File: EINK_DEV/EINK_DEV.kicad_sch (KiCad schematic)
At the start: 33 parts, among them J1 FPC, J2 USB_B_Micro, Q1 NMOS, U1 STM32WB55CEUx, U2 TP4056-42-ESOP8

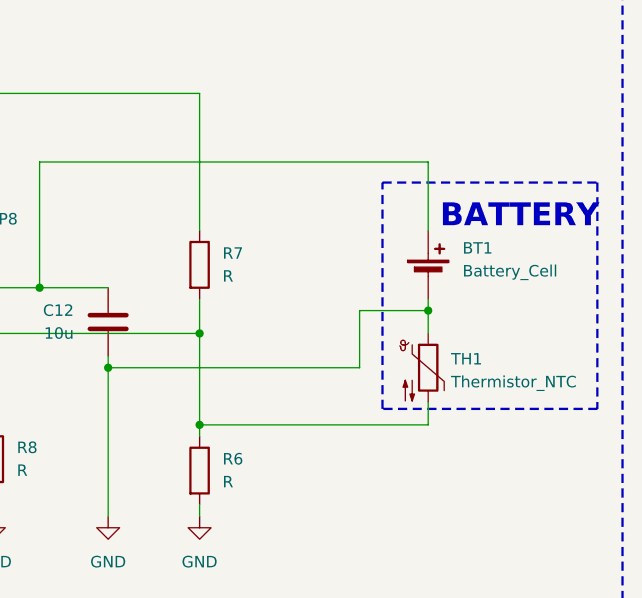
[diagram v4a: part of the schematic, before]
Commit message: Add connector instead of battery
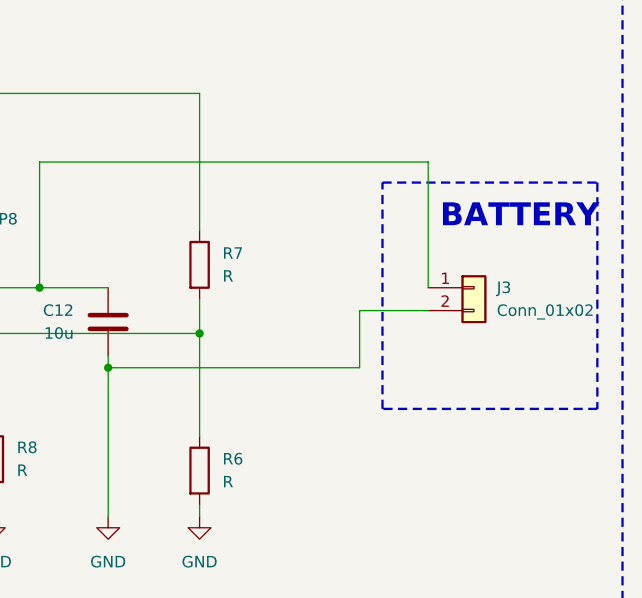
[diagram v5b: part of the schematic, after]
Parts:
- removed BT1: Battery_Cell, symbol Device:Battery_Cell
- removed TH1: Thermistor_NTC, symbol Device:Thermistor_NTC
- added J3: Conn_01x02, symbol Connector_Generic:Conn_01x02
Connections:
- net GND: now also J3.2 (Pin_2)
- net at C12.2, U2.5 (BAT): now also J3.1 (Pin_1)
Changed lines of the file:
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@@
 	)
 	(junction
-		(at 237.49 100.33)
-		(diameter 0)
-		(color 0 0 0 0)
-	)
-	(junction
 		(at 237.49 90.17)
 		(diameter 0)
@@
 	)
 	(junction
-		(at 262.89 87.63)
-		(diameter 0)
-		(color 0 0 0 0)
-	)
-	(junction
 		(at 219.71 85.09)
 		(diameter 0)
@@
 	(wire
 		(pts
-			(xy 237.49 100.33) (xy 237.49 101.6)
+			(xy 237.49 90.17) (xy 237.49 101.6)
 		)
 		(stroke
@@
 	(wire
 		(pts
-			(xy 262.89 86.36) (xy 262.89 87.63)
-		)
-		(stroke
-			(width 0)
-			(type default)
-		)
-	)
-	(wire
-		(pts
 			(xy 189.23 92.71) (xy 160.02 92.71)
 		)
@@
 	(wire
 		(pts
-			(xy 262.89 87.63) (xy 262.89 90.17)
-		)
-		(stroke
-			(width 0)
-			(type default)
-		)
-	)
-	(wire
-		(pts
 			(xy 99.06 149.86) (xy 99.06 152.4)
 		)
@@
 	(wire
 		(pts
-			(xy 237.49 90.17) (xy 237.49 100.33)
-		)
-		(stroke
-			(width 0)
-			(type default)
-		)
-	)
-	(wire
-		(pts
 			(xy 160.02 63.5) (xy 160.02 69.85)
 		)
@@
 	(wire
 		(pts
-			(xy 237.49 100.33) (xy 262.89 100.33)
-		)
-		(stroke
-			(width 0)
-			(type default)
-		)
-	)
-	(wire
-		(pts
-			(xy 262.89 100.33) (xy 262.89 97.79)
-		)
-		(stroke
-			(width 0)
-			(type default)
-		)
-	)
-	(wire
-		(pts
 			(xy 154.94 186.69) (xy 158.75 186.69)
 		)
@@
 	(wire
 		(pts
-			(xy 262.89 71.12) (xy 262.89 78.74)
+			(xy 262.89 71.12) (xy 262.89 85.09)
 		)
 		(stroke
@@
 	)
 	(symbol
-		(lib_id "Device:Thermistor_NTC")
-		(at 262.89 93.98 0)
-		(unit 1)
-		(exclude_from_sim no)
-		(in_bom yes)
-		(on_board yes)
-		(dnp no)
-		(fields_autoplaced yes)
-		(property "Reference" "TH1"
-			(at 265.43 93.0274 0)
-			(effects
-				(font
-					(size 1.27 1.27)
-				)
-				(justify left)
-			)
-		)
-		(property "Value" "Thermistor_NTC"
-			(at 265.43 95.5674 0)
-			(effects
-				(font
-					(size 1.27 1.27)
-				)
-				(justify left)
-			)
-		)
-		(property "Footprint" ""
-			(at 262.89 92.71 0)
-			(effects
-				(font
-					(size 1.27 1.27)
-				)
-				(hide yes)
-			)
-		)
-		(property "Datasheet" "~"
-			(at 262.89 92.71 0)
-			(effects
-				(font
-					(size 1.27 1.27)
-				)
-				(hide yes)
-			)
-		)
-		(property "Description" "Temperature dependent resistor, negative temperature coefficient"
-			(at 262.89 93.98 0)
-			(effects
-				(font
-					(size 1.27 1.27)
-				)
-				(hide yes)
-			)
-		)
-		(pin "1"
-		)
-		(pin "2"
-		)
-		(instances
-			(project ""
-				(path "/21ffd272-94a2-4b6a-9954-5d1217824b1f"
-					(reference "TH1")
-					(unit 1)
-				)
-			)
-		)
-	)
-	(symbol
 		(lib_id "Device:D")
 		(at 90.17 152.4 0)
@@
 	)
 	(symbol
-		(lib_id "Device:Battery_Cell")
-		(at 262.89 83.82 0)
-		(unit 1)
-		(exclude_from_sim no)
-		(in_bom yes)
-		(on_board yes)
-		(dnp no)
-		(fields_autoplaced yes)
-		(property "Reference" "BT1"
-			(at 266.7 80.7084 0)
-			(effects
-				(font
-					(size 1.27 1.27)
-				)
-				(justify left)
-			)
-		)
-		(property "Value" "Battery_Cell"
-			(at 266.7 83.2484 0)
-			(effects
-				(font
-					(size 1.27 1.27)
-				)
-				(justify left)
-			)
-		)
-		(property "Footprint" ""
-			(at 262.89 82.296 90)
-			(effects
-				(font
-					(size 1.27 1.27)
-				)
-				(hide yes)
-			)
-		)
-		(property "Datasheet" "~"
-			(at 262.89 82.296 90)
-			(effects
-				(font
-					(size 1.27 1.27)
-				)
-				(hide yes)
-			)
-		)
-		(property "Description" "Single-cell battery"
-			(at 262.89 83.82 0)
-			(effects
-				(font
-					(size 1.27 1.27)
-				)
-				(hide yes)
-			)
-		)
-		(pin "1"
-		)
-		(pin "2"
-		)
-		(instances
-			(project ""
-				(path "/21ffd272-94a2-4b6a-9954-5d1217824b1f"
-					(reference "BT1")
-					(unit 1)
-				)
-			)
-		)
-	)
-	(symbol
 		(lib_id "Device:C")
 		(at 227.33 88.9 0)
@@
 					(unit 1)
 				)
+			)
+		)
+	)
+	(symbol
+		(lib_id "Connector_Generic:Conn_01x02")
+		(at 267.97 85.09 0)
+		(unit 1)
+		(exclude_from_sim no)
+		(in_bom yes)
+		(on_board yes)
+		(dnp no)
+		(fields_autoplaced yes)
+		(property "Reference" "J3"
+			(at 270.51 85.0899 0)
+			(effects
+				(font
+					(size 1.27 1.27)
+				)
+				(justify left)
+			)
+		)
+		(property "Value" "Conn_01x02"
+			(at 270.51 87.6299 0)
+			(effects
+				(font
+					(size 1.27 1.27)
+				)
+				(justify left)
+			)
+		)
+		(property "Footprint" ""
+			(at 267.97 85.09 0)
+			(effects
+				(font
+					(size 1.27 1.27)
+				)
+				(hide yes)
+			)
+		)
+		(property "Datasheet" "~"
+			(at 267.97 85.09 0)
+			(effects
+				(font
+					(size 1.27 1.27)
+				)
+				(hide yes)
+			)
+		)
+		(property "Description" "Generic connector, single row, 01x02, script generated (kicad-library-utils/schlib/autogen/connector/)"
+			(at 267.97 85.09 0)
+			(effects
+				(font
+					(size 1.27 1.27)
+				)
+				(hide yes)
+			)
+		)
+		(pin "1"
+		)
+		(pin "2"
+		)
+		(instances
+			(project ""
+				(path "/21ffd272-94a2-4b6a-9954-5d1217824b1f"
+					(reference "J3")
+					(unit 1)
+				)

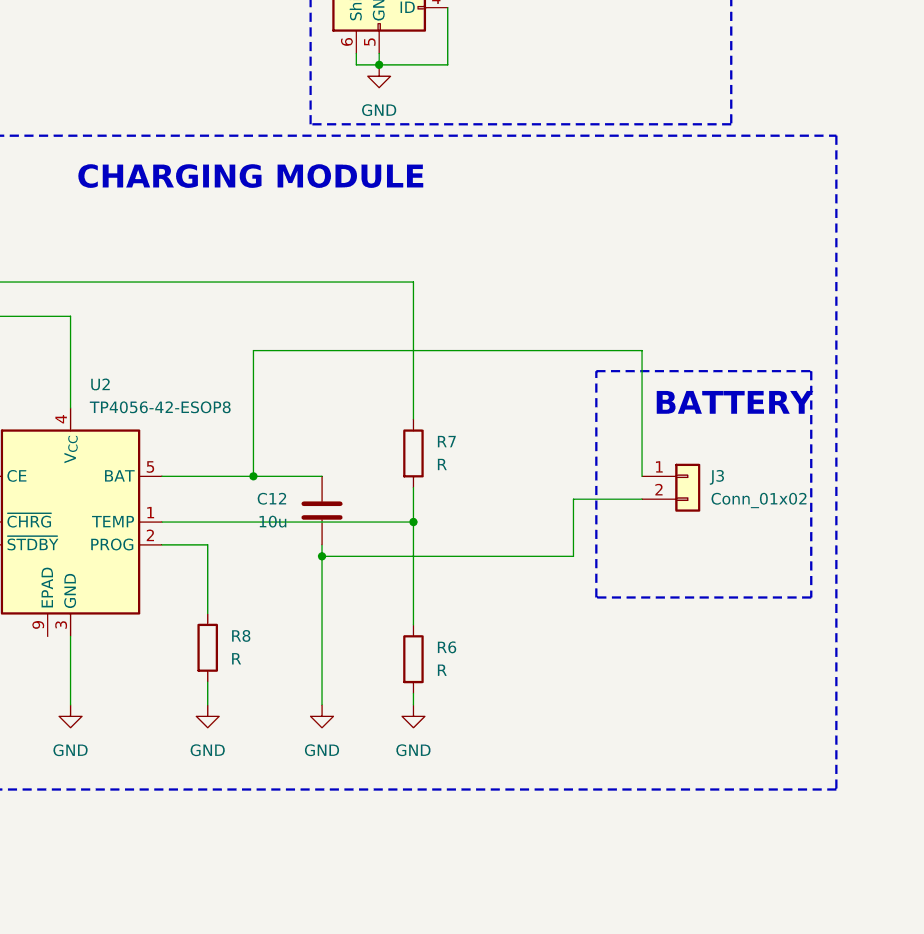
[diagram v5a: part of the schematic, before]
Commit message: Add options for baterry connector
2Pin and 3Pin Connector are available. Depends on a jumper placing.
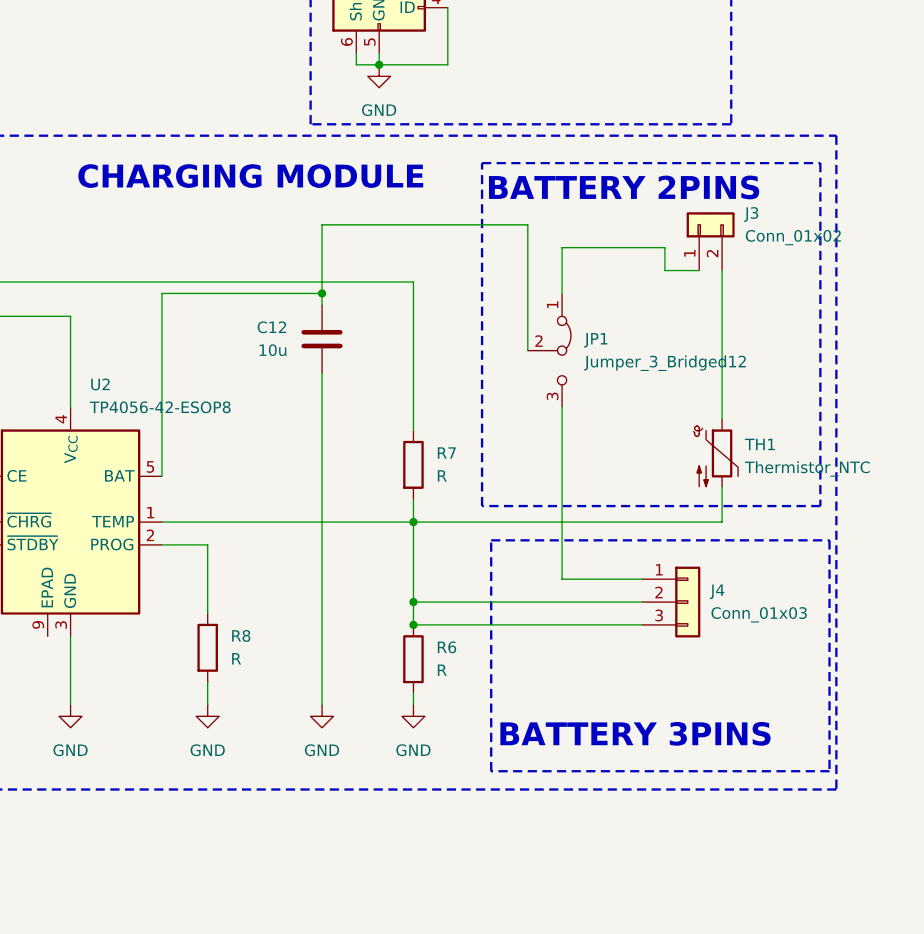
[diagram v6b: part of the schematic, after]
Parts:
- added J4: Conn_01x03, symbol Connector_Generic:Conn_01x03
- added JP1: Jumper_3_Bridged12, symbol Jumper:Jumper_3_Bridged12
- added TH1: Thermistor_NTC, symbol Device:Thermistor_NTC
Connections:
- net GND: no longer J3.2 (Pin_2)
- net at R6.1, R7.2, U2.1 (TEMP): now also J4.2 (Pin_2), J4.3 (Pin_3), TH1.2
- net at C12.2, U2.5 (BAT): now also JP1.2 (C); no longer J3.1 (Pin_1)
- new net: J3.1 (Pin_1), JP1.1 (A)
- new net: J3.2 (Pin_2), TH1.1
- new net: J4.1 (Pin_1), JP1.3 (B)
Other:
- note added: "BATTERY 2PINS"
- note added: "BATTERY 3PINS"
- note removed: "BATTERY"
- moved on the sheet: C12, R7

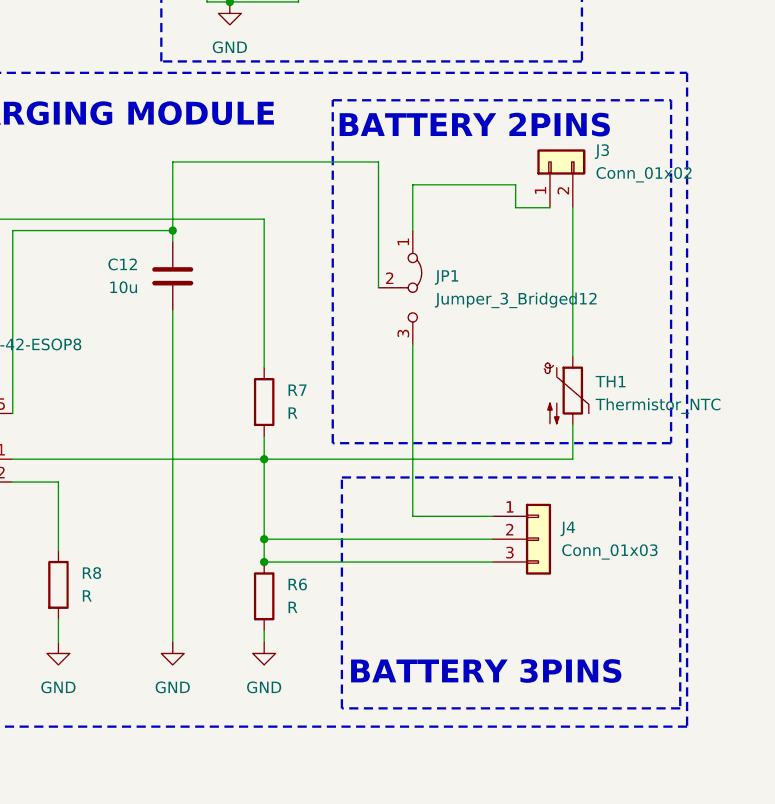
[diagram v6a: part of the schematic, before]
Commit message: Add onnections from battery to BAT pin
Add connections from 2 and 3Pin connectors to BAT pin.
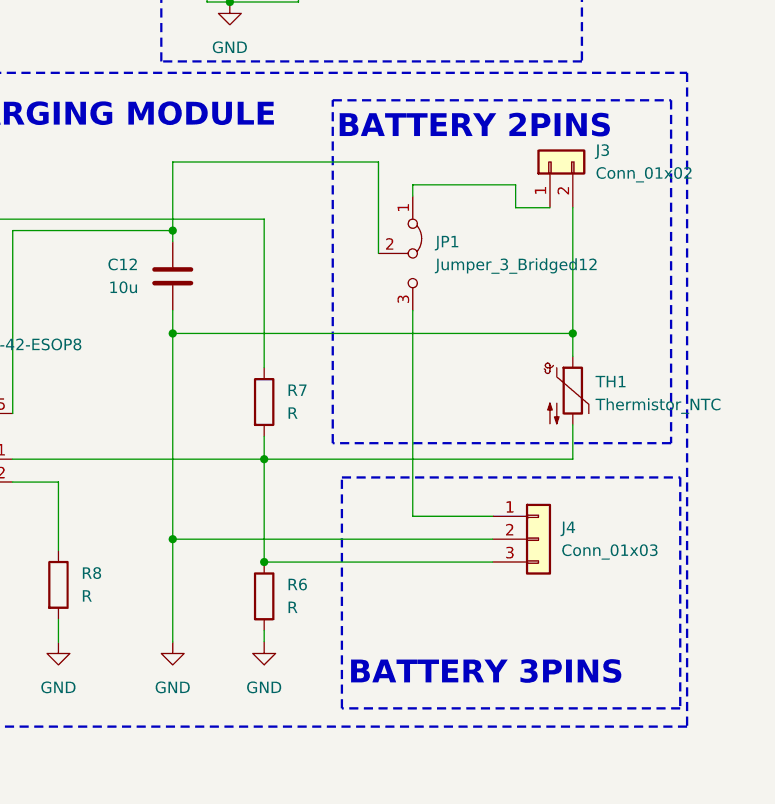
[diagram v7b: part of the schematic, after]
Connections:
- net GND: now also J3.2 (Pin_2), J4.2 (Pin_2), TH1.1
- net at J4.3 (Pin_3), R6.1, R7.2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: no longer J4.2 (Pin_2)
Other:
- moved on the sheet: JP1
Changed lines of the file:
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@@
 	)
 	(junction
+		(at 227.33 99.06)
+		(diameter 0)
+		(color 0 0 0 0)
+	)
+	(junction
 		(at 69.85 179.07)
 		(diameter 0)
@@
 	)
 	(junction
-		(at 237.49 99.06)
+		(at 271.78 76.2)
+		(diameter 0)
+		(color 0 0 0 0)
+	)
+	(junction
+		(at 227.33 76.2)
 		(diameter 0)
 		(color 0 0 0 0)
@@
 	(wire
 		(pts
-			(xy 250.19 57.15) (xy 250.19 71.12)
+			(xy 250.19 57.15) (xy 250.19 67.31)
 		)
 		(stroke
@@
 	(wire
 		(pts
+			(xy 227.33 99.06) (xy 227.33 110.49)
+		)
+		(stroke
+			(width 0)
+			(type default)
+		)
+	)
+	(wire
+		(pts
 			(xy 154.94 179.07) (xy 158.75 179.07)
 		)
@@
 	(wire
 		(pts
-			(xy 237.49 99.06) (xy 262.89 99.06)
+			(xy 254 59.69) (xy 254 60.96)
 		)
 		(stroke
@@
 	(wire
 		(pts
-			(xy 254 59.69) (xy 254 64.77)
+			(xy 154.94 130.81) (xy 158.75 130.81)
 		)
 		(stroke
@@
 	(wire
 		(pts
-			(xy 154.94 130.81) (xy 158.75 130.81)
+			(xy 99.06 144.78) (xy 99.06 142.24)
 		)
 		(stroke
@@
 	(wire
 		(pts
-			(xy 99.06 144.78) (xy 99.06 142.24)
+			(xy 160.02 87.63) (xy 160.02 92.71)
 		)
 		(stroke
@@
 	(wire
 		(pts
-			(xy 160.02 87.63) (xy 160.02 92.71)
+			(xy 124.46 166.37) (xy 133.35 166.37)
 		)
 		(stroke
@@
 	(wire
 		(pts
-			(xy 124.46 166.37) (xy 133.35 166.37)
+			(xy 254 59.69) (xy 265.43 59.69)
 		)
 		(stroke
@@
 	(wire
 		(pts
-			(xy 254 59.69) (xy 265.43 59.69)
+			(xy 173.99 78.74) (xy 173.99 80.01)
 		)
 		(stroke
@@
 	(wire
 		(pts
-			(xy 173.99 78.74) (xy 173.99 80.01)
+			(xy 227.33 76.2) (xy 271.78 76.2)
 		)
 		(stroke
@@
 	(wire
 		(pts
-			(xy 254 77.47) (xy 254 96.52)
+			(xy 254 73.66) (xy 254 96.52)
 		)
 		(stroke
@@
 	(wire
 		(pts
-			(xy 237.49 90.17) (xy 237.49 99.06)
+			(xy 237.49 90.17) (xy 237.49 101.6)
 		)
 		(stroke
@@
 	(wire
 		(pts
+			(xy 227.33 99.06) (xy 262.89 99.06)
+		)
+		(stroke
+			(width 0)
+			(type default)
+		)
+	)
+	(wire
+		(pts
 			(xy 138.43 179.07) (xy 144.78 179.07)
 		)
@@
 	(wire
 		(pts
-			(xy 227.33 73.66) (xy 227.33 110.49)
+			(xy 227.33 73.66) (xy 227.33 76.2)
 		)
 		(stroke
@@
 	(wire
 		(pts
-			(xy 271.78 62.23) (xy 271.78 78.74)
+			(xy 271.78 62.23) (xy 271.78 76.2)
 		)
 		(stroke
@@
 	(wire
 		(pts
-			(xy 237.49 99.06) (xy 237.49 101.6)
+			(xy 154.94 161.29) (xy 158.75 161.29)
 		)
 		(stroke
@@
 	(wire
 		(pts
-			(xy 154.94 161.29) (xy 158.75 161.29)
+			(xy 124.46 173.99) (xy 128.27 173.99)
 		)
 		(stroke
@@
 	(wire
 		(pts
-			(xy 124.46 173.99) (xy 128.27 173.99)
+			(xy 227.33 76.2) (xy 227.33 99.06)
 		)
 		(stroke
@@
 		)
 	)
+	(wire
+		(pts
+			(xy 271.78 76.2) (xy 271.78 78.74)
+		)
+		(stroke
+			(width 0)
+			(type default)
+		)
+	)
 	(global_label "VGH"
 		(shape bidirectional)
@@
 	(symbol
 		(lib_id "Jumper:Jumper_3_Bridged12")
-		(at 254 71.12 270)
+		(at 254 67.31 270)
 		(unit 1)
 		(exclude_from_sim no)
@@
 		(on_board yes)
 		(dnp no)
-		(fields_autoplaced yes)
 		(property "Reference" "JP1"
-			(at 256.54 69.8499 90)
+			(at 256.54 66.0399 90)
 			(effects
 				(font
@@
 		)
 		(property "Value" "Jumper_3_Bridged12"
-			(at 256.54 72.3899 90)
+			(at 256.54 68.5799 90)
 			(effects
 				(font
@@
 		)
 		(property "Footprint" ""
-			(at 254 71.12 0)
+			(at 254 67.31 0)
 			(effects
 				(font
@@
 		)
 		(property "Datasheet" "~"
-			(at 254 71.12 0)
+			(at 254 67.31 0)
 			(effects
 				(font
@@
 		)
 		(property "Description" "Jumper, 3-pole, pins 1+2 closed/bridged"
-			(at 254 71.12 0)
+			(at 254 67.31 0)
 			(effects
 				(font

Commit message: Added BATT protection
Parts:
- added C13: ~, symbol Device:C
- added R10: ~, symbol Device:R
- added R9: R, symbol Device:R
- added U3: DW01A, Package_TO_SOT_SMD:SOT-23-6, symbol Battery_Management:DW01A
- added U4: ~, symbol Battery_Management:FS8205A
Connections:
- net GND: now also C13.2, U3.6 (GND), U4.1 (S1)
- net +BATT: now reaches C12.2, JP1.2 (C), U2.5 (BAT)
- net +BATT: now also R10.1
- new net: R9.1, U3.2 (CS)
- new net: C13.1, R10.2, U3.5 (VCC)
- new net: U3.3 (OC), U4.4 (G2)
- new net: U3.1 (OD), U4.6 (G1)
- new net -BATT: R9.2, U4.3 (S2)
- no-connect marks 4 -> 6
